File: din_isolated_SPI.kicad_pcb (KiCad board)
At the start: 2 copper layers, 32.5 x 58.7 mm, 4 parts, among them U1 SI8661AB-B-IS1, U2 MCP7940N, U3 BME280, U4 WeMos_mini

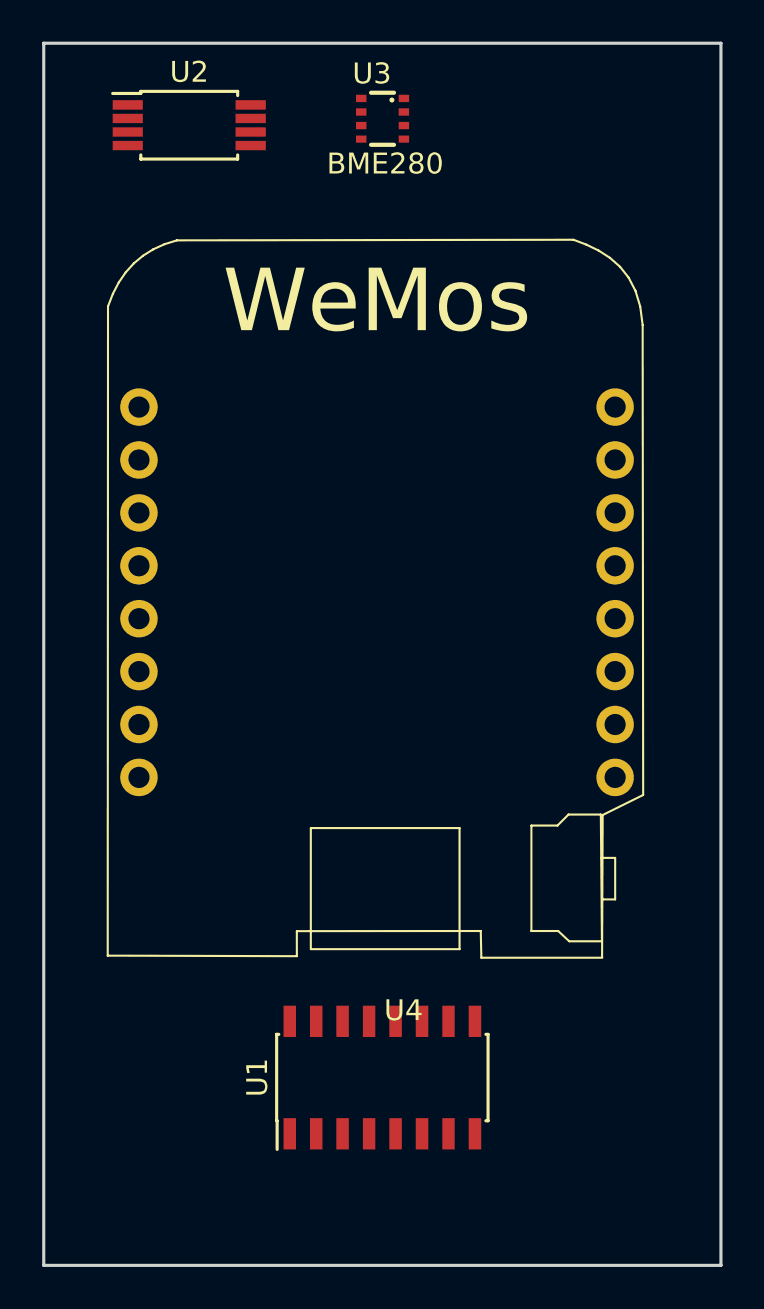
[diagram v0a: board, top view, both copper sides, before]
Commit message: Autorouted basic isolated SPI
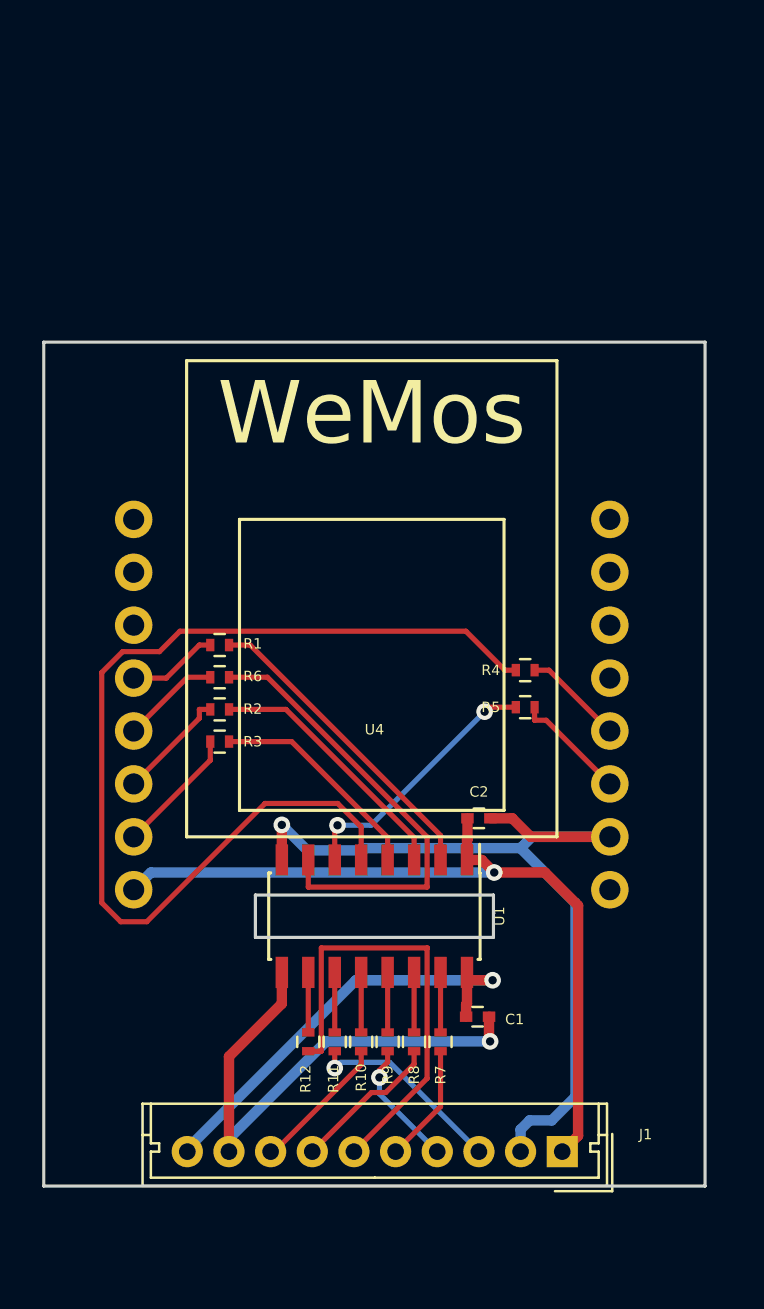
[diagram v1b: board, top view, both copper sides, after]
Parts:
- removed U2: MCP7940N, Housings_SSOP:TSSOP-8_4.4x3mm_Pitch0.65mm
- removed U3: BME280, BME280
- added C1: 100nF, Capacitors_SMD:C_0402, F.Cu at (137.7, 83.3)
- added C2: 100nF, Capacitors_SMD:C_0402, F.Cu at (137.7, 73.8)
- added J1: CONN_01X10, Connectors_Molex:Molex_MicroLatch-53253-1070_10x2.00mm_Straight, F.Cu at (141.7, 89.8)
- added R1: 50R, Resistors_SMD:R_0402, F.Cu at (125.3, 65.5)
- added R10: 50R, Resistors_SMD:R_0402, F.Cu at (132.1, 84.5)
- added R11: 50R, Resistors_SMD:R_0402, F.Cu at (130.8, 84.5)
- added R12: 50R, Resistors_SMD:R_0402, F.Cu at (129.5, 84.5)
- added R2: 50R, Resistors_SMD:R_0402, F.Cu at (125.3, 68.6)
- added R3: 50R, Resistors_SMD:R_0402, F.Cu at (125.3, 70.1)
- added R4: 50R, Resistors_SMD:R_0402, F.Cu at (140.0, 66.7)
- added R5: 50R, Resistors_SMD:R_0402, F.Cu at (140.0, 68.5)
- added R6: 50R, Resistors_SMD:R_0402, F.Cu at (125.3, 67.0)
- added R7: 50R, Resistors_SMD:R_0402, F.Cu at (135.9, 84.5)
- added R8: 50R, Resistors_SMD:R_0402, F.Cu at (134.6, 84.5)
- added R9: 50R, Resistors_SMD:R_0402, F.Cu at (133.3, 84.5)
- U4: moved to B.Cu
- moved U1 7.76 mm to (132.7, 78.5), turned to 270 degrees
- moved U4 5.40 mm to (132.6, 69.6), turned to 180 degrees
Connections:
- U1 pad 1: Net-(U1-Pad1) -> 3V3_C
- U1 pad 16: Net-(U1-Pad16) -> 3V3_I
- U1 pad 8: Net-(U1-Pad8) -> GND_C
- U1 pad 9: Net-(U1-Pad9) -> GND_I
- U4 pad 12: Net-(U4-Pad12) -> CLK_W
- U4 pad 13: Net-(U4-Pad13) -> MISO_W
- U4 pad 14: Net-(U4-Pad14) -> MOSI_W
- U4 pad 15: Net-(U4-Pad15) -> CS0_W
- U4 pad 16: Net-(U4-Pad16) -> 3V3_C
- U4 pad 2: Net-(U4-Pad2) -> GND_C
- U4 pad 3: Net-(U4-Pad3) -> CS2_W
- U4 pad 4: Net-(U4-Pad4) -> CS1_W
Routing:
- net Net-(R4-Pad1): track 0.00 -> 49.8 mm
- net GND_C: track 0.00 -> 41.7 mm, vias 0 -> 1
- net 3V3_C: track 0.00 -> 38.0 mm, vias 0 -> 1
- net GND_I: track 0.00 -> 26.0 mm, vias 0 -> 1
- net Net-(R6-Pad1): track 0.00 -> 22.1 mm
- net MISO_E: track 0.00 -> 21.9 mm
- net 3V3_I: track 0.00 -> 21.5 mm, vias 0 -> 1
- net Net-(R1-Pad1): track 0.00 -> 15.1 mm
- net Net-(R5-Pad1): track 0.00 -> 12.6 mm, vias 0 -> 2
- net Net-(R2-Pad1): track 0.00 -> 12.5 mm
- net Net-(R3-Pad1): track 0.00 -> 10.6 mm
- net CS2_E: track 0.00 -> 9.62 mm, vias 0 -> 1
- net MOSI_E: track 0.00 -> 7.25 mm
- net CS1_E: track 0.00 -> 6.72 mm
- net CS0_E: track 0.00 -> 6.13 mm, vias 0 -> 1
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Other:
- board size 32.5 x 58.7 mm -> 31.8 x 40.5 mm
- net class Power added: clearance 0.5, trace_width 0.5, via_dia 0.8, via_drill 0.4

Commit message: Added logos
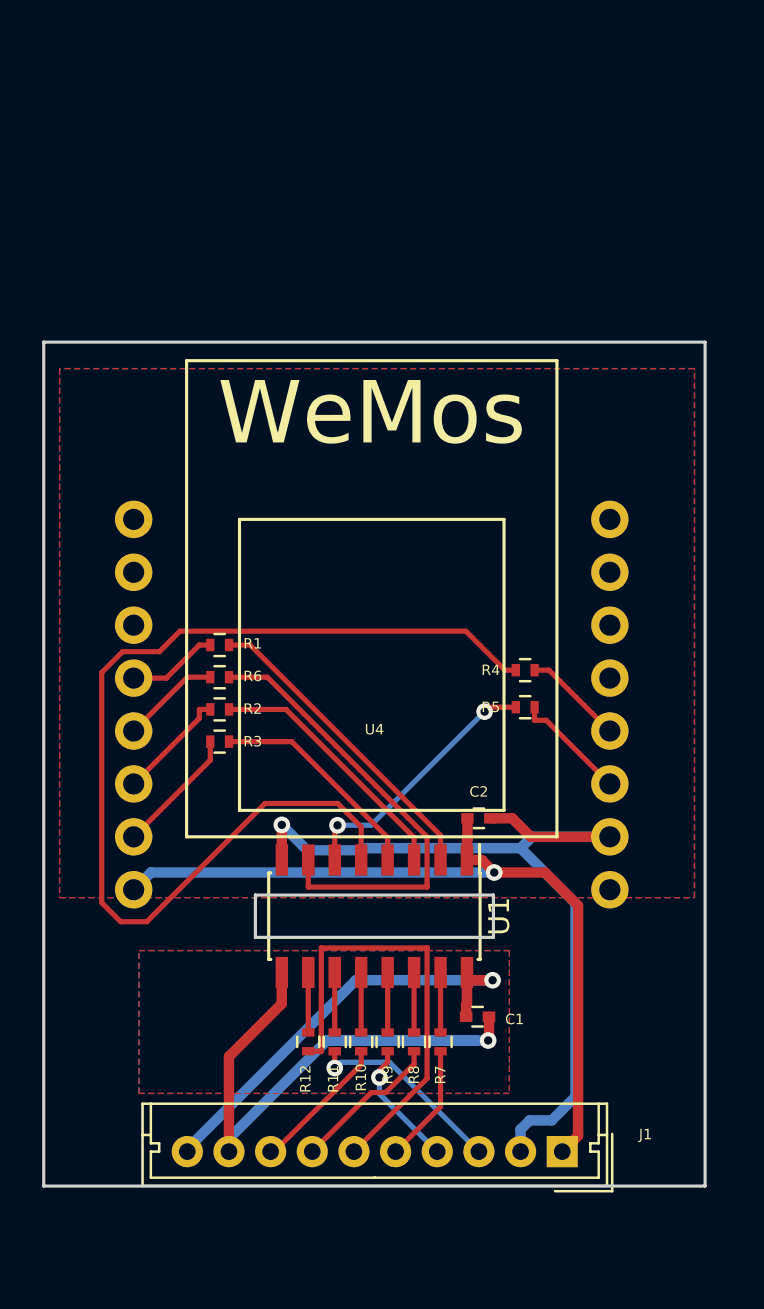
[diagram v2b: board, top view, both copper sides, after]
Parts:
- added G1: LOGO, Whatnick_logo:Whatnick_logo, B.Cu at (132.6, 59.3)
- added LOGO1: Logo_Open_Hardware_Small, Symbols:OSHW-Symbol_6.7x6mm_SilkScreen, B.Cu at (132.8, 66.0)
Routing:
- net GND_I: track 26.0 -> 33.0 mm
- added copper zone on B.Cu, net GND_C
- added copper zone on F.Cu, net GND_C
- added copper zone on B.Cu, net GND_I
- added copper zone on F.Cu, net GND_I
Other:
- net class Default: clearance 0.2 -> 0.15
- rule trace_clearance: 0.2 -> 0.15
- rule trace_min: 0.2 -> 0.15
- board text added: "Wemos Isolated SPI Basic v0.1 30/10/2017"

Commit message: Added stitching vias and silk screen detail
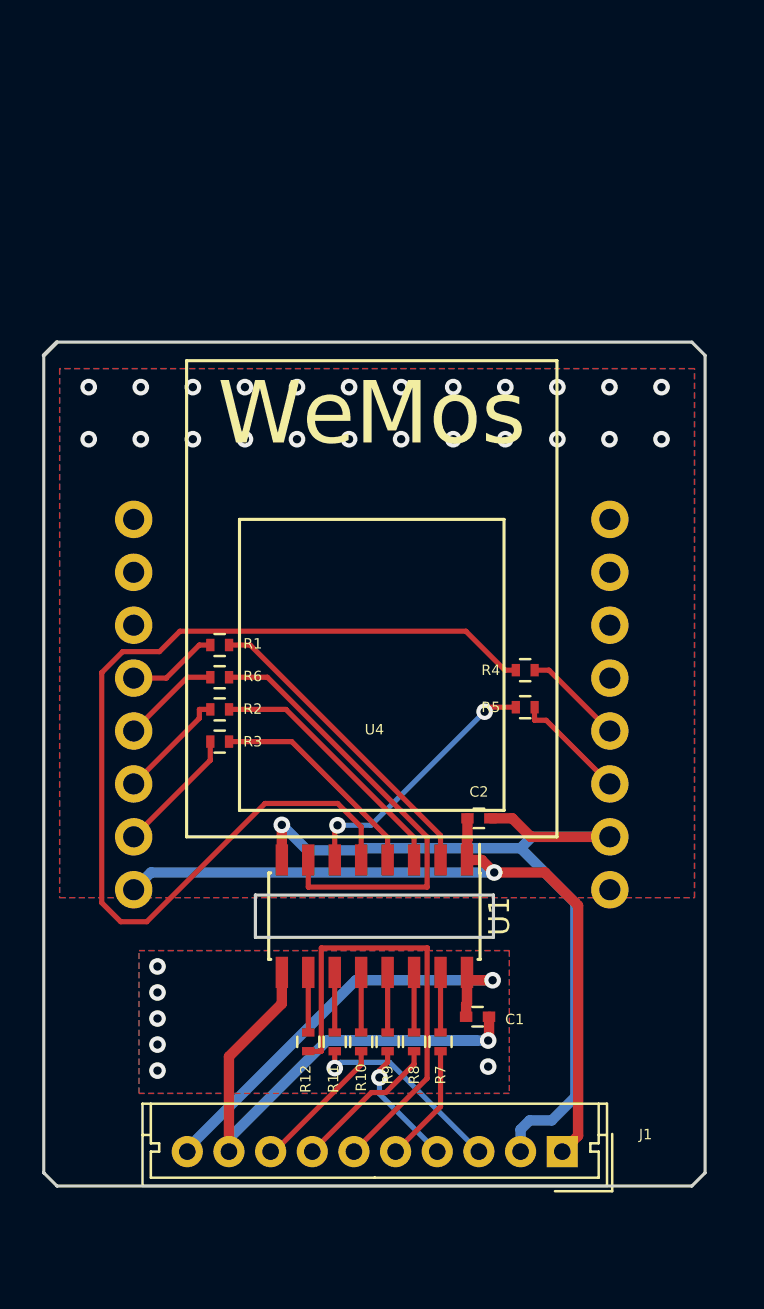
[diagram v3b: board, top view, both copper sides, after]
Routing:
- net GND_I: vias 1 -> 7
- net GND_C: vias 1 -> 25
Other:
- outline, holes or cut-outs redrawn
- board text added: "3V3"
- board text added: "3V3_C"
- board text added: "3V3_I"
- board text added: "5V"
- board text added: "A0"
- board text added: "CLK"
- board text added: "CS0"
- board text added: "CS1"
- board text added: "CS2"
- board text added: "D0"
- board text added: "D1"
- board text added: "D2"
- board text added: "D3"
- board text added: "D4"
- board text added: "D5"
- board text added: "D6"
- board text added: "D7"
- board text added: "D8"
- board text added: "GND"
- board text added: "GND_C"
- board text added: "GND_I"
- board text added: "MISO"
- board text added: "MOSI"
- board text added: "RX"
- board text added: "TX"
- board text added: "~RST"
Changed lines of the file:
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@@
-(kicad_pcb (version 20170123) (host pcbnew "(2017-06-19 revision 6733101c6)-makepkg")
+(kicad_pcb (version 20170919) (host pcbnew "(2017-09-19 revision dddaa7e69)-makepkg")
   (general
-    (links 34)
-    (no_connects 0)
-    (area 116.764999 49.2885 148.665001 94.1815)
     (thickness 1.6)
-    (drawings 10)
-    (tracks 131)
+    (drawings 40)
+    (tracks 161)
     (zones 0)
     (modules 19)
@@
       (layerselection 0x00030_ffffffff)
       (usegerberextensions false)
+      (usegerberattributes true)
+      (usegerberadvancedattributes true)
+      (creategerberjobfile true)
       (excludeedgelayer true)
       (linewidth 0.100000)
@@
     )
   )
+  (gr_line (start 147.955 91.44) (end 148.59 90.805) (layer Edge.Cuts) (width 0.15))
+  (gr_line (start 116.84 90.805) (end 117.475 91.44) (layer Edge.Cuts) (width 0.15))
+  (gr_line (start 147.955 50.927) (end 148.59 51.562) (layer Edge.Cuts) (width 0.15))
+  (gr_line (start 117.475 50.927) (end 116.84 51.562) (layer Edge.Cuts) (width 0.2))
+  (gr_text TX (at 146.685 59.69) (layer B.SilkS)
+    (effects (font (size 0.8 0.8) (thickness 0.2)) (justify mirror))
+  )
+  (gr_text D1 (at 146.685 64.77) (layer B.SilkS)
+    (effects (font (size 0.8 0.8) (thickness 0.2)) (justify mirror))
+  )
+  (gr_text D4 (at 146.685 72.39) (layer B.SilkS)
+    (effects (font (size 0.8 0.8) (thickness 0.2)) (justify mirror))
+  )
+  (gr_text RX (at 146.685 62.23) (layer B.SilkS)
+    (effects (font (size 0.8 0.8) (thickness 0.2)) (justify mirror))
+  )
+  (gr_text D3 (at 146.685 69.85) (layer B.SilkS)
+    (effects (font (size 0.8 0.8) (thickness 0.2)) (justify mirror))
+  )
+  (gr_text D2 (at 146.685 67.31) (layer B.SilkS)
+    (effects (font (size 0.8 0.8) (thickness 0.2)) (justify mirror))
+  )
+  (gr_text 5V (at 146.685 77.47) (layer B.SilkS)
+    (effects (font (size 0.8 0.8) (thickness 0.2)) (justify mirror))
+  )
+  (gr_text GND (at 146.685 74.93) (layer B.SilkS)
+    (effects (font (size 0.8 0.8) (thickness 0.2)) (justify mirror))
+  )
+  (gr_text 3V3 (at 118.491 77.343) (layer B.SilkS)
+    (effects (font (size 0.8 0.8) (thickness 0.2)) (justify mirror))
+  )
+  (gr_text D8 (at 118.491 74.803) (layer B.SilkS)
+    (effects (font (size 0.8 0.8) (thickness 0.2)) (justify mirror))
+  )
+  (gr_text D7 (at 118.491 72.263) (layer B.SilkS)
+    (effects (font (size 0.8 0.8) (thickness 0.2)) (justify mirror))
+  )
+  (gr_text D6 (at 118.491 69.723) (layer B.SilkS)
+    (effects (font (size 0.8 0.8) (thickness 0.2)) (justify mirror))
+  )
+  (gr_text D5 (at 118.491 67.183) (layer B.SilkS)
+    (effects (font (size 0.8 0.8) (thickness 0.2)) (justify mirror))
+  )
+  (gr_text D0 (at 118.491 64.643) (layer B.SilkS)
+    (effects (font (size 0.8 0.8) (thickness 0.2)) (justify mirror))
+  )
+  (gr_text A0 (at 118.491 62.103) (layer B.SilkS)
+    (effects (font (size 0.8 0.8) (thickness 0.2)) (justify mirror))
+  )
+  (gr_text ~RST (at 118.491 59.563) (layer B.SilkS)
+    (effects (font (size 0.8 0.8) (thickness 0.2)) (justify mirror))
+  )
+  (gr_text 3V3_I (at 123.605 87.376 90) (layer B.SilkS)
+    (effects (font (size 0.5 0.5) (thickness 0.12)) (justify mirror))
+  )
+  (gr_text GND_I (at 125.605 87.376 90) (layer B.SilkS)
+    (effects (font (size 0.5 0.5) (thickness 0.12)) (justify mirror))
+  )
+  (gr_text CS1 (at 127.605 87.376 90) (layer B.SilkS)
+    (effects (font (size 0.5 0.5) (thickness 0.12)) (justify mirror))
+  )
+  (gr_text MOSI (at 129.605 87.376 90) (layer B.SilkS)
+    (effects (font (size 0.5 0.5) (thickness 0.12)) (justify mirror))
+  )
+  (gr_text MISO (at 131.605 87.376 90) (layer B.SilkS)
+    (effects (font (size 0.5 0.5) (thickness 0.12)) (justify mirror))
+  )
+  (gr_text CLK (at 133.605 87.376 90) (layer B.SilkS)
+    (effects (font (size 0.5 0.5) (thickness 0.12)) (justify mirror))
+  )
+  (gr_text CS0 (at 135.605 87.376 90) (layer B.SilkS)
+    (effects (font (size 0.5 0.5) (thickness 0.12)) (justify mirror))
+  )
+  (gr_text "CS2\n" (at 137.605 87.376 90) (layer B.SilkS)
+    (effects (font (size 0.5 0.5) (thickness 0.12)) (justify mirror))
+  )
+  (gr_text GND_C (at 139.605 87.376 90) (layer B.SilkS)
+    (effects (font (size 0.5 0.5) (thickness 0.12)) (justify mirror))
+  )
+  (gr_text 3V3_C (at 141.605 87.376 90) (layer B.SilkS)
+    (effects (font (size 0.5 0.5) (thickness 0.12)) (justify mirror))
+  )
   (gr_text "Wemos Isolated SPI\nBasic v0.1 30/10/2017" (at 132.715 70.993) (layer B.SilkS)
     (effects (font (size 1 1) (thickness 0.25)) (justify mirror))
@@
   (gr_line (start 138.43 77.47) (end 138.43 79.502) (layer Edge.Cuts) (width 0.15))
   (gr_line (start 127 77.47) (end 138.43 77.47) (layer Edge.Cuts) (width 0.15))
-  (gr_line (start 116.84 91.44) (end 116.84 50.927) (layer Edge.Cuts) (width 0.15))
-  (gr_line (start 148.59 91.44) (end 116.84 91.44) (layer Edge.Cuts) (width 0.15))
-  (gr_line (start 148.59 50.927) (end 148.59 91.44) (layer Edge.Cuts) (width 0.15))
-  (gr_line (start 116.84 50.927) (end 148.59 50.927) (layer Edge.Cuts) (width 0.15))
+  (gr_line (start 116.84 90.805) (end 116.84 51.562) (layer Edge.Cuts) (width 0.15))
+  (gr_line (start 147.955 91.44) (end 117.475 91.44) (layer Edge.Cuts) (width 0.15))
+  (gr_line (start 148.59 51.562) (end 148.59 90.805) (layer Edge.Cuts) (width 0.15))
+  (gr_line (start 117.475 50.927) (end 147.955 50.927) (layer Edge.Cuts) (width 0.15))
   (segment (start 140.9603 69.0783) (end 140.404 69.0783) (width 0.25) (layer F.Cu) (net 9))
   (segment (start 144.018 72.136) (end 140.9603 69.0783) (width 0.25) (layer F.Cu) (net 9) (status 10))
@@
   (segment (start 132.9563 86.2272) (end 132.9563 85.8875) (width 0.25) (layer F.Cu) (net 33))
   (segment (start 133.35 84.9685) (end 133.35 85.4938) (width 0.25) (layer F.Cu) (net 33) (status 10))
+  (via (at 146.499 55.586) (size 0.8) (layers F.Cu B.Cu) (net 34))
+  (via (at 143.999 55.586) (size 0.8) (layers F.Cu B.Cu) (net 34))
+  (via (at 141.499 55.586) (size 0.8) (layers F.Cu B.Cu) (net 34))
+  (via (at 138.999 55.586) (size 0.8) (layers F.Cu B.Cu) (net 34))
+  (via (at 136.499 55.586) (size 0.8) (layers F.Cu B.Cu) (net 34))
+  (via (at 133.999 55.586) (size 0.8) (layers F.Cu B.Cu) (net 34))
+  (via (at 131.499 55.586) (size 0.8) (layers F.Cu B.Cu) (net 34))
+  (via (at 128.999 55.586) (size 0.8) (layers F.Cu B.Cu) (net 34))
+  (via (at 126.499 55.586) (size 0.8) (layers F.Cu B.Cu) (net 34))
+  (via (at 123.999 55.586) (size 0.8) (layers F.Cu B.Cu) (net 34))
+  (via (at 121.499 55.586) (size 0.8) (layers F.Cu B.Cu) (net 34))
+  (via (at 118.999 55.586) (size 0.8) (layers F.Cu B.Cu) (net 34))
+  (via (at 146.499 53.086) (size 0.8) (layers F.Cu B.Cu) (net 34))
+  (via (at 143.999 53.086) (size 0.8) (layers F.Cu B.Cu) (net 34))
+  (via (at 141.499 53.086) (size 0.8) (layers F.Cu B.Cu) (net 34))
+  (via (at 138.999 53.086) (size 0.8) (layers F.Cu B.Cu) (net 34))
+  (via (at 136.499 53.086) (size 0.8) (layers F.Cu B.Cu) (net 34))
+  (via (at 133.999 53.086) (size 0.8) (layers F.Cu B.Cu) (net 34))
+  (via (at 131.499 53.086) (size 0.8) (layers F.Cu B.Cu) (net 34))
+  (via (at 128.999 53.086) (size 0.8) (layers F.Cu B.Cu) (net 34))
+  (via (at 126.499 53.086) (size 0.8) (layers F.Cu B.Cu) (net 34))
+  (via (at 123.999 53.086) (size 0.8) (layers F.Cu B.Cu) (net 34))
+  (via (at 121.499 53.086) (size 0.8) (layers F.Cu B.Cu) (net 34))
+  (via (at 118.999 53.086) (size 0.8) (layers F.Cu B.Cu) (net 34))
   (segment (start 139.732 88.72834) (end 139.732 89.789) (width 0.5) (layer B.Cu) (net 34) (status 20))
   (segment (start 141.232001 88.288999) (end 140.171341 88.288999) (width 0.5) (layer B.Cu) (net 34))
@@
   (segment (start 129.4894 75.3223) (end 132.0163 75.3223) (width 0.5) (layer B.Cu) (net 34))
   (segment (start 128.27 74.1029) (end 129.4894 75.3223) (width 0.5) (layer B.Cu) (net 34))
+  (via (at 138.176 85.70501) (size 0.8) (drill 0.4) (layers F.Cu B.Cu) (net 35))
+  (via (at 122.301 85.899) (size 0.8) (drill 0.4) (layers F.Cu B.Cu) (net 35))
+  (via (at 122.301 84.649) (size 0.8) (drill 0.4) (layers F.Cu B.Cu) (net 35))
+  (via (at 122.301 83.399) (size 0.8) (drill 0.4) (layers F.Cu B.Cu) (net 35))
+  (via (at 122.301 82.149) (size 0.8) (drill 0.4) (layers F.Cu B.Cu) (net 35))
+  (via (at 122.301 80.899) (size 0.8) (drill 0.4) (layers F.Cu B.Cu) (net 35))
   (segment (start 130.44239 84.45501) (end 137.610315 84.45501) (width 0.5) (layer B.Cu) (net 35))
   (segment (start 138.218 83.312) (end 138.218 84.41301) (width 0.5) (layer F.Cu) (net 35) (status 10))
